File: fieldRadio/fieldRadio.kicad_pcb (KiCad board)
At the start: 4 copper layers, 275.4 x 190.9 mm, 488 parts, among them IC1 UCC27517DBVR, IC2 UCC27517DBVR, IC3 SN74LVC1G04DBVT, IC4 SN74AUP2G79DCUR, IC5 TS5A23157, IC6 SN74CBTLV3253, IC7 INA821ID, IC8 INA821ID, J1 Barrel_Jack_Switch, J10 Conn_01x03, J11 Conn_01x04, J2 5227161-3, J3 Conn_01x03, J4 AudioJack2_Switch, J5 AudioJack3_Switch, J6 AudioJack2_Switch, J7 Conn_01x04, J8 Conn_01x11, J9 Conn_01x16, Q1 MMBT3904, Q10 BSS123, Q11 BSS123, Q12 DMN10H220LPDW, Q13 NSS1C301ET4G, Q14 BSS123, Q15 BSS123, Q16 BSS123, Q17 BSS123, Q18 BSS123, Q19 MOSFET-NCHANNELBSS138, Q2 MMBT3904, Q20 J309, Q21 IRF9540, Q3 PMV240SP, Q4 MMBT3904, Q5 PMV240SP, Q6 BSS123, Q7 BSS123, Q8 BSS123, Q9 BSS123, T1 1:1, T2 T50-TRIFILAR, U1 MIC5235-5.0YM5, U10 LM1085-5.0, U11 OPA1679, U12 OPA1679, U13 OPA1679, U2 OPA1678, U3 OPA1678, U4 OPA1678, U5 OPA1678, U6 LM386, U7 MIC5219-3.3YM5, U8 Si5351A-B-GT, U9 MCP1802x-xx02xOT, Y1 32.768kHz, Y2 25MHz

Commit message: Placement of preselector and qsd
Finished placement of these two blocks
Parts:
- removed L13, L14, L15, L16, L26, L38: 47uH, Inductor_THT:L_Axial_L13.0mm_D4.5mm_P15.24mm_Horizontal_Fastron_HCCC
- added L41: B78148E1473J000, SamacSys_Parts:B78148E, F.Cu at (262.9, 147.8)
- added L42: B78148E1473J000, SamacSys_Parts:B78148E, F.Cu at (279.6, 140.3)
- added L43: B78148E1473J000, SamacSys_Parts:B78148E, F.Cu at (270.9, 68.2)
- added L44: B78148E1473J000, SamacSys_Parts:B78148E, F.Cu at (271.2, 63.2)
- added L45: B78148E1473J000, SamacSys_Parts:B78148E, F.Cu at (155.1, 65.7)
- added L46: B78148E1473J000, SamacSys_Parts:B78148E, F.Cu at (185.2, 65.4)
- C100, C101, C102, C103, C104, C140, C141, C143, C144, C93, C94, C95, C96, C97, C98, C99, Q14, Q15, Q16, Q17, Q18, R140, R141, R79, R80, R82, R83, R84, R85, R86, R87, R88: moved to B.Cu
- L1, L12, L2, L23, L24, L25, L27, L28, L3, L37, L39, L4, L40, L5, L6: value 47uH -> B78148E1473J000; footprint Inductor_THT:L_Axial_L13.0mm_D4.5mm_P15.24mm_Horizontal_Fastron_HCCC -> SamacSys_Parts:B78148E
- moved L30 516.4 mm to (308.2, 134.2), turned to 180 degrees
- moved L29 507.0 mm to (293.8, 134.2), turned to 180 degrees
- moved L34 504.0 mm to (308.2, 137.6)
- moved D24 498.6 mm to (316.8, 146.7), turned to 180 degrees
- moved D20 496.9 mm to (317.0, 124.9), turned to 180 degrees
- moved L33 493.7 mm to (293.8, 137.6)
- moved R86 482.3 mm to (319.3, 135.9), turned to 90 degrees
- moved L27 478.9 mm to (284.3, 131.7), turned to 90 degrees
- moved R84 476.1 mm to (311.2, 135.9), turned to -90 degrees
- moved Q16 474.5 mm to (314.3, 135.9)
- moved L32 473.8 mm to (270.2, 134.2), turned to 180 degrees
- moved L39 473.4 mm to (284.4, 140.2), turned to -90 degrees
- moved D23 471.6 mm to (285.4, 146.5)
- moved D19 469.0 mm to (284.6, 124.9)
- moved C94 467.8 mm to (311.5, 131.4), turned to 90 degrees
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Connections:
- L1 pad 1: Net-(Q5-D) -> Net-(L1-Pad1)
- L1 pad 2: Net-(D1-A) -> Net-(D10-A)
- L12 pad 1: Net-(C16-Pad1) -> Net-(Q16-D)
- L12 pad 2: Net-(Q7-D) -> Net-(D20-K)
- L2 pad 1: Net-(L2-Pad1) -> Net-(C16-Pad1)
- L2 pad 2: Net-(D1-K) -> Net-(Q7-D)
- L23 pad 1: Net-(L23-Pad1) -> Net-(D2-A)
- L23 pad 2: /qsd/rf_in -> Net-(Q3-D)
- L24 pad 1: Net-(L24-Pad1) -> Net-(Q5-D)
- L24 pad 2: /Preselector/input -> Net-(D1-A)
- L25 pad 1: Net-(D19-K) -> Net-(Q14-D)
- L25 pad 2: Net-(Q15-D) -> Net-(D22-K)
- L27 pad 1: Net-(D21-K) -> Net-(Q15-D)
- L27 pad 2: Net-(Q17-D) -> Net-(D19-K)
- L28 pad 1: Net-(D22-K) -> Net-(Q14-D)
- L28 pad 2: Net-(Q14-D) -> Net-(D26-K)
- L3 pad 1: Net-(D2-A) -> Net-(C17-Pad1)
- L3 pad 2: Net-(Q3-D) -> Net-(Q8-D)
- L37 pad 1: Net-(D23-K) -> Net-(L37-Pad1)
- L37 pad 2: Net-(Q15-D) -> /qsd/rf_in
- L39 pad 1: Net-(D25-K) -> Net-(Q15-D)
- L39 pad 2: Net-(Q17-D) -> Net-(D23-K)
- L4 pad 1: Net-(L4-Pad1) -> Net-(C18-Pad1)
- L4 pad 2: Net-(D5-K) -> Net-(Q9-D)
- L40 pad 1: Net-(D26-K) -> Net-(Q17-D)
- L40 pad 2: Net-(Q14-D) -> Net-(D21-K)
- L5 pad 2: Net-(D10-A) -> /LPF/trswitch
- L6 pad 1: Net-(L6-Pad1) -> Net-(Q16-D)
- L6 pad 2: /LPF/trswitch -> Net-(D24-K)
- R12 pad 1: Net-(L2-Pad1) -> Net-(L44-Pad1)
- R14 pad 1: Net-(L4-Pad1) -> Net-(L43-Pad1)
- R15 pad 2: Net-(L5-Pad1) -> Net-(L1-Pad1)
- R16 pad 2: Net-(L6-Pad1) -> Net-(L5-Pad1)
- R78 pad 2: Net-(L23-Pad1) -> Net-(L37-Pad1)
- R81 pad 2: Net-(L24-Pad1) -> Net-(L41-Pad1)

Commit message: Finished Groups
Blocks are placed
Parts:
- C111, C113, C115, C116, C120, C124, C126, C128, C130, C163, C164, C166, C43, C46, C59, C62, C63, C66, C75, C80, C85, C86, C90, C91, L22, R100, R101, R104, R105, R108, R109, R112, R117, R118, R120, R121, R125, R126, R129, R130, R34, R40, R61, R62, R66, R67, R74, R76, R77, R96, R97: moved to B.Cu
- moved L22 581.9 mm to (400.5, 103.8), turned to 90 degrees
- moved T1 560.4 mm to (384.6, 78.9)
- moved C52 542.2 mm to (376.1, 100.8), turned to 180 degrees
- moved VR1 542.2 mm to (369.0, 116.1)
- moved Q13 539.9 mm to (384.9, 108.4)
- moved C53 539.7 mm to (387.7, 102.6), turned to -90 degrees
- moved C42 538.4 mm to (382.0, 97.5), turned to 90 degrees
- moved C54 536.4 mm to (384.8, 102.8), turned to -90 degrees
- moved C45 535.7 mm to (380.4, 97.5), turned to -90 degrees
- moved Q12 535.3 mm to (389.3, 86.5), turned to -90 degrees
- moved C44 534.2 mm to (381.3, 75.5), turned to -90 degrees
- moved C55 533.7 mm to (380.7, 113.4), turned to 180 degrees
- moved C56 533.1 mm to (380.7, 115.7), turned to 180 degrees
- moved C40 532.3 mm to (376.7, 87.0), turned to 90 degrees
- moved C47 532.0 mm to (378.7, 97.6), turned to -90 degrees
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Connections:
- C43 pad 2: Net-(U$1E-V-) -> GND
- C46 pad 1: Net-(U$1E-V-) -> GND
- C51 pad 2: Net-(U$1E-V-) -> GND
- IC1 pad 2: Net-(IC1-GND) -> GND
- IC1 pad 4: Net-(IC1-GND) -> GND
- IC2 pad 2: Net-(IC1-GND) -> GND
- R36 pad 2: Net-(U$1E-V-) -> GND
- U$1 pad 11: Net-(U$1E-V-) -> GND

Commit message: Initial Block Placement
Initial blocks are placed roughly
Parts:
- moved L22 317.0 mm to (85.9, 142.8), turned to 0 degrees
- moved C56 305.0 mm to (75.9, 128.0), turned to 90 degrees
- moved C55 302.8 mm to (78.2, 128.0), turned to 90 degrees
- moved Q13 302.6 mm to (83.2, 132.2), turned to -90 degrees
- moved C53 300.5 mm to (89.0, 135.0), turned to 180 degrees
- moved C54 297.4 mm to (88.8, 132.0), turned to 180 degrees
- moved R39 294.7 mm to (80.8, 122.5), turned to 90 degrees
- moved R37 292.6 mm to (82.9, 122.5), turned to -90 degrees
- moved R38 290.2 mm to (85.5, 122.5), turned to 90 degrees
- moved C42 289.7 mm to (94.2, 129.3), turned to 0 degrees
- moved Q12 288.5 mm to (105.2, 136.6), turned to 180 degrees
- moved C45 288.0 mm to (94.1, 127.7), turned to 180 degrees
- moved C52 286.2 mm to (90.8, 123.4), turned to 90 degrees
- moved C47 286.1 mm to (94.0, 126.0), turned to 180 degrees
- moved IC2 284.1 mm to (98.4, 127.7), turned to 0 degrees
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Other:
- board size 275.4 x 190.9 mm -> 159 x 159 mm

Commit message: Placement Refinement 1
Ungrouping blocks and optimizing placement
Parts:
- removed C52: CAP_POLPTH1, Capacitor_THT:C_Radial_D5.0mm_H11.0mm_P2.00mm
- C145, C146: value 470pF -> 330pF
- C154, C156, C53, C54, Q12, R37, R38, R39: moved to B.Cu
- C3, C4, Q1, Q2, Q3, Q4, Q5, Q6, R1, R10, R11, R2, R3, R4, R5, R6, R7, R8, R9: moved to F.Cu
- L22: footprint Transformer_THT:Autotransformer_Toroid_1Tap_Horizontal_D14.0mm_Amidon-T50 -> Transformer_THT:Transformer_Toroid_Horizontal_D14.0mm_Amidon-T50; moved to F.Cu
- R147, R148: value 49.9 -> 499
- R75: value 33k -> 10k
- moved C2 144.3 mm to (177.8, 209.9)
- moved C1 143.3 mm to (176.9, 215.7)
- moved C83 54.3 mm to (277.6, 104.4)
- moved C72 54.3 mm to (297.7, 99.0)
- moved R73 54.3 mm to (275.1, 93.8)
- moved U6 54.3 mm to (261.5, 102.9)
- moved C71 54.3 mm to (290.1, 110.2)
- moved C74 54.3 mm to (270.6, 99.7)
- moved C75 54.3 mm to (288.8, 100.0)
- moved C79 54.3 mm to (280.8, 104.6)
- moved C84 54.3 mm to (276.1, 96.3)
- moved C86 54.3 mm to (255.5, 97.3)
- moved C92 54.3 mm to (247.0, 99.2)
- moved R68 54.3 mm to (285.7, 104.6)
- moved R70 54.3 mm to (285.7, 98.3)
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
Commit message: Refine Placement 2
Finish refining block placement; ready for initial routing work.
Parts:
- removed C152, C75: 0.1uF, Capacitor_SMD:C_0603_1608Metric_Pad1.08x0.95mm_HandSolder
- removed R142: 10k, Resistor_SMD:R_0603_1608Metric_Pad0.98x0.95mm_HandSolder
- removed R64, R65: 10K, Resistor_SMD:R_0603_1608Metric_Pad0.98x0.95mm_HandSolder
- C118, C119, C123, C129, C131, C132, C147, C148, C2, C74, C84, C87, R102, R103, R106, R107, R113, R114, R115, R116, R119, R124, R131, R132, R143, R144, R145, R146, R73: moved to B.Cu
- C124, C126, C86, R125, R126, R129, R130, R66, R67: moved to F.Cu
- moved C82 116.6 mm to (168.9, 119.8), turned to 180 degrees
- moved R90 115.3 mm to (91.7, 214.1), turned to 0 degrees
- moved R89 113.8 mm to (91.7, 215.7), turned to 180 degrees
- moved C72 113.4 mm to (184.7, 107.9), turned to 180 degrees
- moved C105 112.2 mm to (91.7, 217.4), turned to 0 degrees
- moved R63 111.7 mm to (184.8, 109.6), turned to 0 degrees
- moved R73 111.6 mm to (167.3, 122.8), turned to -90 degrees
- moved C80 110.9 mm to (182.5, 121.7), turned to 90 degrees
- moved C84 110.3 mm to (168.9, 122.7), turned to 90 degrees
- moved C76 109.9 mm to (181.5, 130.2), turned to -90 degrees
- moved R71 109.7 mm to (172.1, 128.3), turned to 90 degrees
- moved C83 109.7 mm to (170.6, 128.3), turned to 90 degrees
- moved C79 109.5 mm to (173.9, 128.3), turned to -90 degrees
- moved R69 109.3 mm to (175.7, 128.3), turned to -90 degrees
- moved C77 109.2 mm to (177.5, 128.3), turned to 90 degrees
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
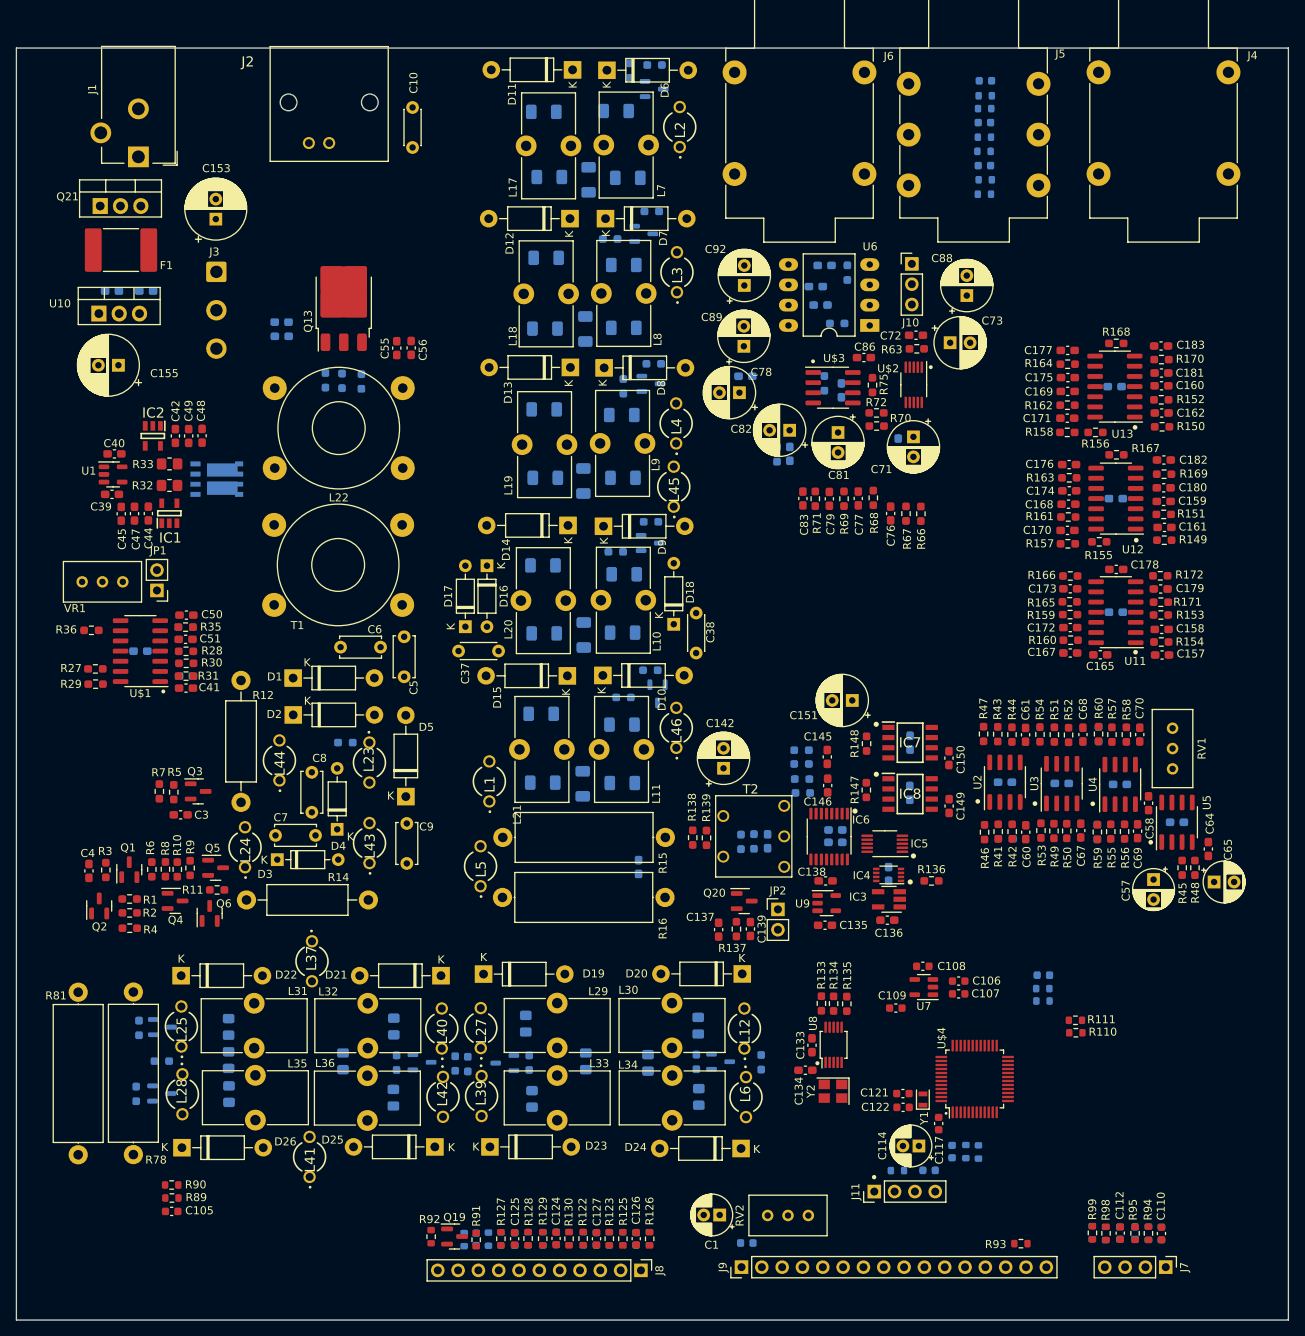
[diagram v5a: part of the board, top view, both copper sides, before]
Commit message: Routing Work 1
Routing blocks
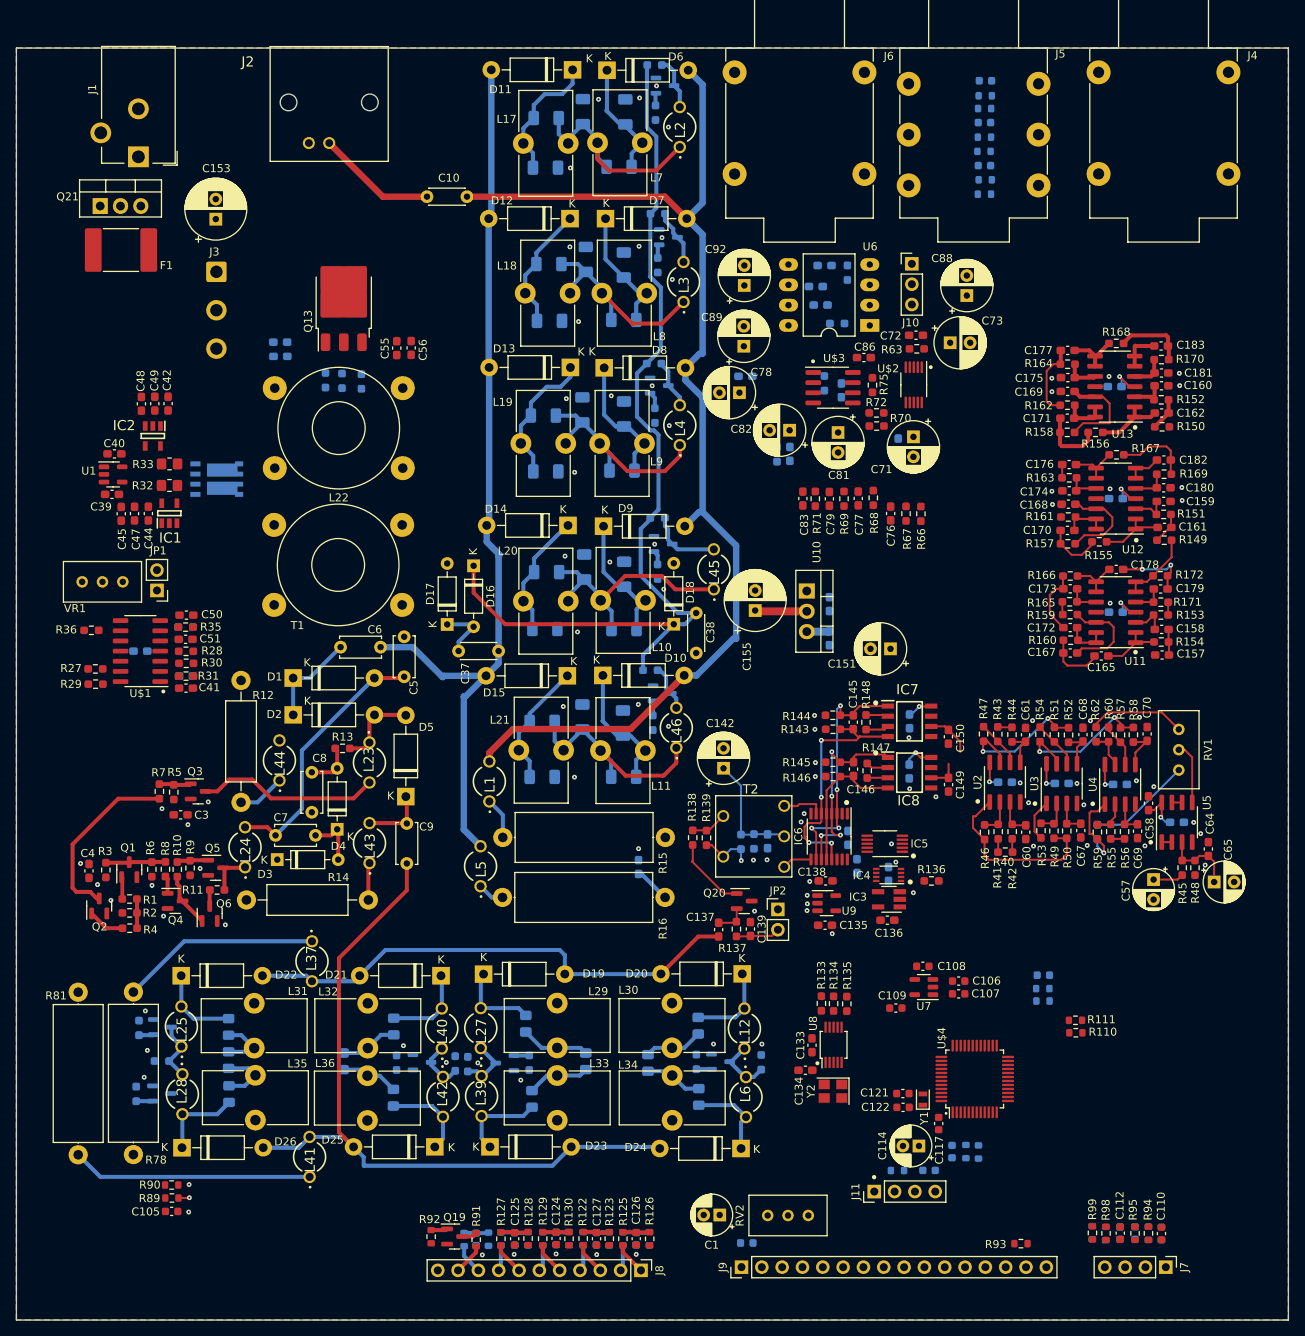
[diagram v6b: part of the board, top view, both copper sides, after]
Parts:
- R13, R143, R144, R145, R146, R40, R62: moved to F.Cu
- moved C156 97.8 mm to (173.9, 141.5), turned to 90 degrees
- moved C154 95.8 mm to (173.9, 145.8), turned to -90 degrees
- moved U10 95.0 mm to (171.1, 139.9), turned to -90 degrees
- moved C155 85.3 mm to (164.6, 142.3), turned to 90 degrees
- moved L45 11.5 mm to (159.4, 137.2)
- moved C48 8.57 mm to (87.9, 116.5), turned to 90 degrees
- moved C27 8.09 mm to (138.8, 99.0), turned to 0 degrees
- moved C151 8.03 mm to (181.5, 147.1)
- moved C28 7.79 mm to (138.1, 117.9), turned to 0 degrees
- moved C29 7.67 mm to (138.5, 137.5), turned to 0 degrees
- moved C30 7.61 mm to (138.0, 156.2), turned to 0 degrees
- moved C26 7.39 mm to (138.5, 80.8), turned to 0 degrees
- moved R23 6.79 mm to (152.4, 99.2), turned to 90 degrees
- moved C10 6.41 mm to (123.6, 90.6), turned to 0 degrees
- moved L7 6.39 mm to (144.9, 83.8), turned to 90 degrees
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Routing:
- net Net-(D10-A): track 0.00 -> 146.6 mm
- net /LPF/HV: track 0.00 -> 118.3 mm
- net /LPF/trswitch: track 0.00 -> 115.6 mm
- net /Preselector/input: track 0.00 -> 93.0 mm
- net /qsd/rf_in: track 0.00 -> 63.5 mm
- net VDD5: track 0.00 -> 51.1 mm, vias 0 -> 12
- net Net-(D1-A): track 0.00 -> 32.8 mm
- net /qsd/0-DEG: track 0.00 -> 31.5 mm, vias 0 -> 4
- net /qsd/180-DEG: track 0.00 -> 31.0 mm, vias 0 -> 4
- net Net-(C19-Pad1): track 0.00 -> 30.8 mm
- net Net-(L41-Pad1): track 0.00 -> 30.1 mm
- net Net-(C20-Pad1): track 0.00 -> 28.3 mm
- net Net-(C18-Pad1): track 0.00 -> 28.2 mm
- net Net-(C16-Pad1): track 0.00 -> 27.5 mm
- net Net-(C17-Pad1): track 0.00 -> 27.1 mm
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- added copper zone on B.Cu, net GND
- added copper zone on F.Cu, net GND
- added copper zone on In1.Cu, net GND
- added copper zone on In2.Cu, net VDD12
- added copper zone on In2.Cu, net VDD5
